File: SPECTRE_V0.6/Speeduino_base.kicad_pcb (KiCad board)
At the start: 2 copper layers, 100 x 93 mm, 234 parts, among them J1 Conn_01x06_Male, J2 Conn_02x04_Odd_Even, Q1 2N7002, Q10 AO3401A, Q11 AO3401A, Q12 BSP78, Q13 BSP78, Q14 BSP78, Q15 BSP78, Q16 BSP78, Q17 SMD-MOSFET-N-CH-55V-2.1A-AO34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, Q18 BSP78, Q19 SMD-MOSFET-N-CH-55V-2.1A-AO34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, Q2 CJ2302, Q20 AO3401A, Q21 BSP78, Q22 AO3401A, Q23 BSP78, Q24 BSP78, Q25 BSP78, Q26 BSP78, Q3 CJ2302, Q4 CJ2302, Q5 CJ2302, Q6 CJ2302, Q7 CJ2302, Q8 SMD-MOSFET-N-CH-55V-2.1A-AO34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, Q9 SMD-MOSFET-N-CH-55V-2.1A-AO34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, U1 MAX9926UAEE+, U10 74LS08, U11 74LS08, U12 TJA1050, U14 MAX3232, U2 LM78M05_TO220, U3 TL431DBZ, U4 74LS32, U5 molex_48pin, U6 LM2901, U7 LTC6992, U8 74LS74, U9 74LS74

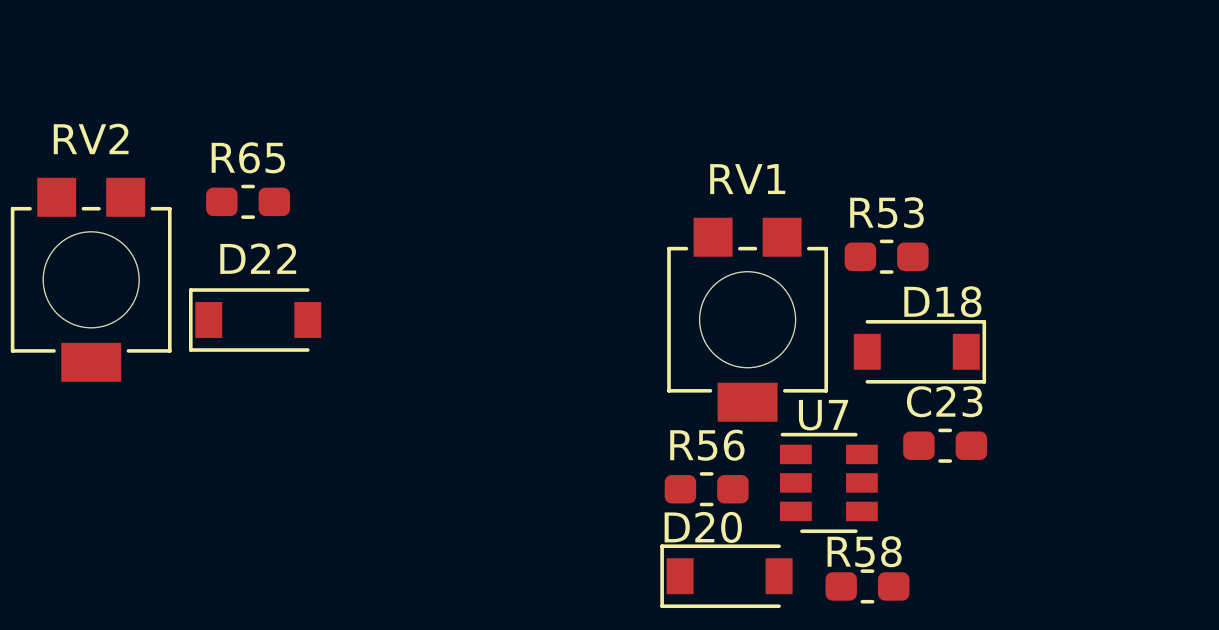
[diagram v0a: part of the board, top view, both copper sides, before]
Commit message: Cleaned and updated the SPECTRE V0.5 Created separate Peak and Hold board.
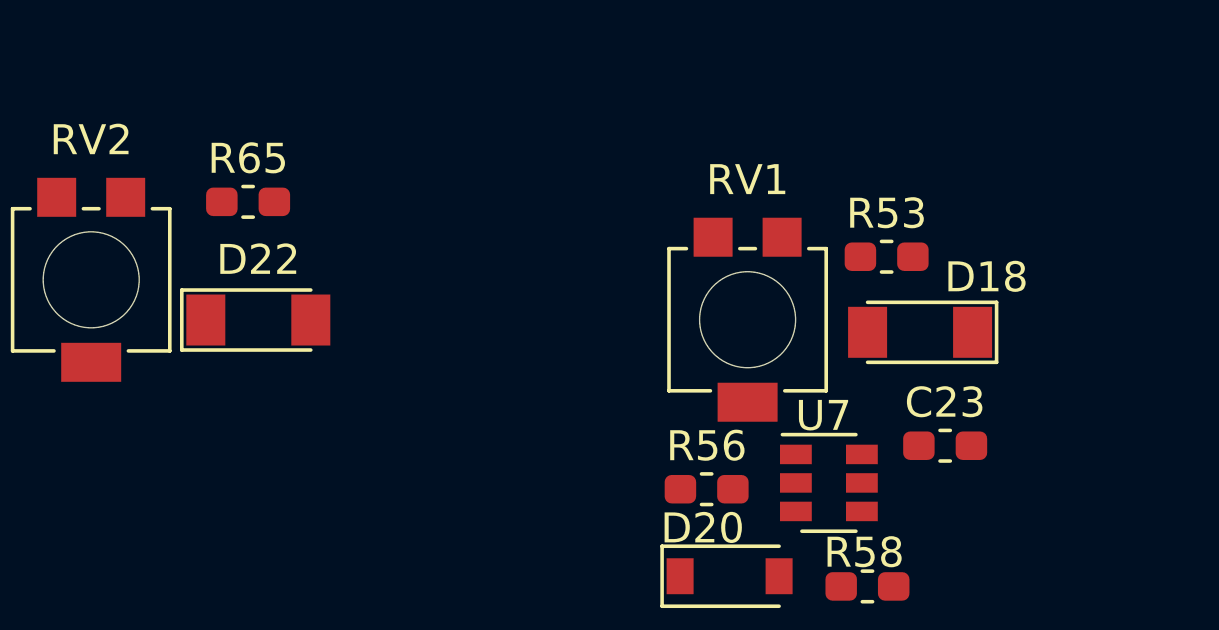
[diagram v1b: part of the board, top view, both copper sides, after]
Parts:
- D18, D22: value SS310 -> LL4148; footprint Diode_SMD:D_SOD-123 -> Diode_SMD:D_MiniMELF
- moved D18 0.66 mm to (127.3, -41.1)
